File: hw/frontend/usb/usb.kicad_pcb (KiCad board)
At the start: 6 copper layers, 100 x 100 mm, 260 parts, among them J1 USB3_MICRO_AB, J2 USB3_MICRO_AB, J3 BARREL_JACK, J4 SAMTEC_QSH-090-D, P4 CONN_1, P5 CONN_1, P6 CONN_1, P7 CONN_1, P8 CONN_1, Q1 MOSFET_P, Q2 MOSFET_P, U1 TUSB1310A, U10 TPS62420, U11 TPS54821, U12 ON_CAT24C256, U13 TCA6416ARTW, U14 TCA6416ARTW, U2 TPS2065C-2, U3 GSG-IP4220CZ6, U4 USB3_ESD_SON50-10, U5 TUSB1310A, U6 TPS2065C-2, U7 GSG-IP4220CZ6, U8 USB3_ESD_SON50-10, U9 MIC5207YM5, X1 40M, X2 40M

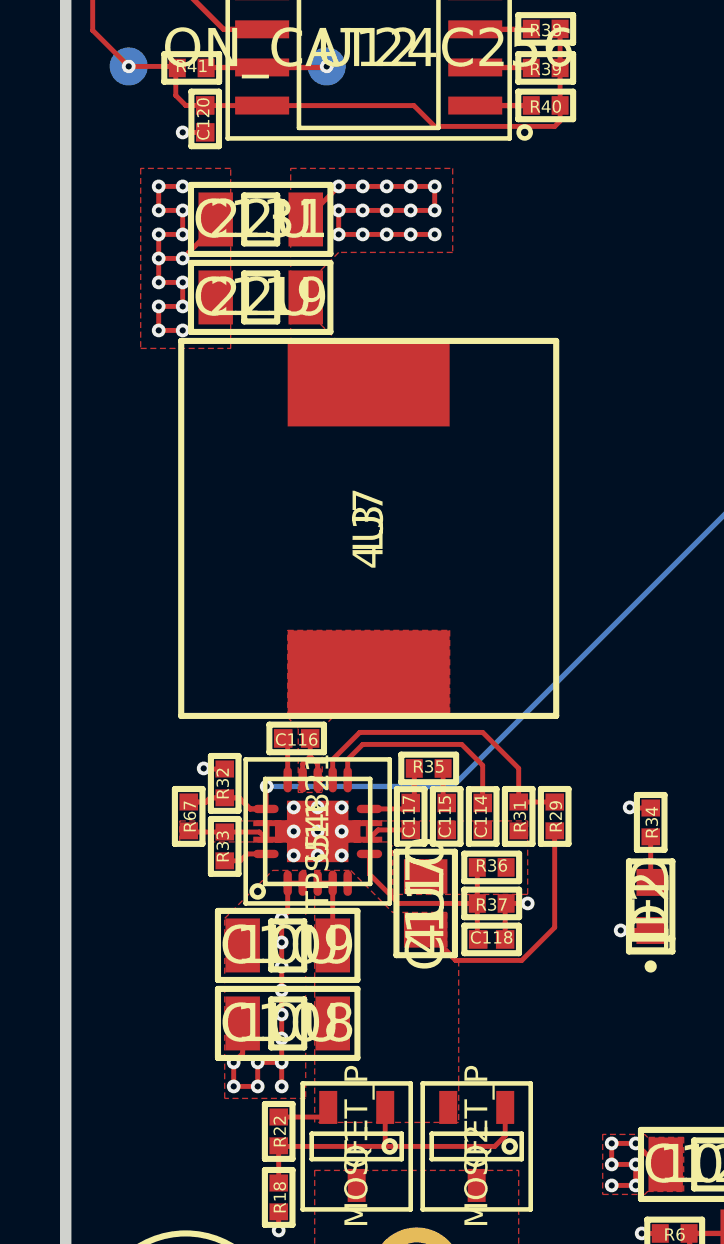
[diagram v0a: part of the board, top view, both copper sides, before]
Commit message: pull ADDR up to VRAW_SW instead of V1P8
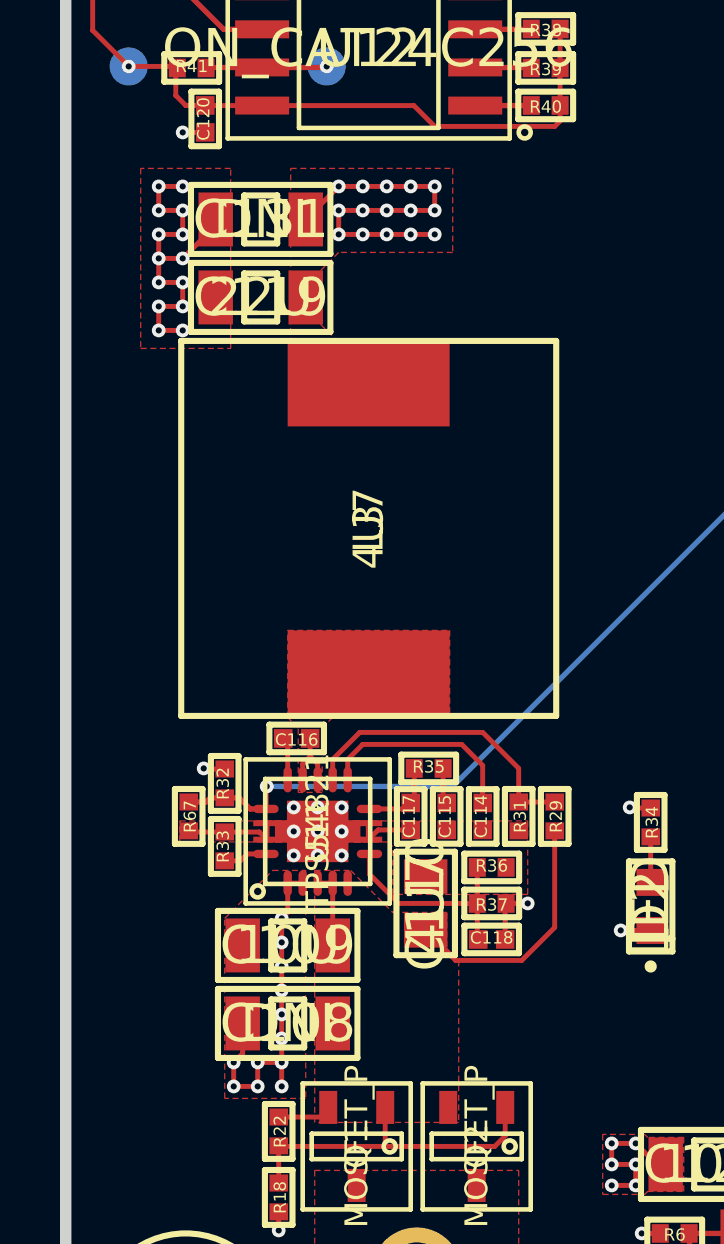
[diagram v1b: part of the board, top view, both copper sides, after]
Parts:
- C108: value 10U -> DNI
- C115: value 27N -> 82N
- C117: value 330P -> 1N5
- C118: value 470P -> 220P
- C131: value 22U -> DNI
- R18, R22: value ? -> 30K
- R21: value ? -> 180K
- R24: value ? -> 360K
- R33: value 86K6 -> 52K3
- R35: value 715R -> 1K58
- R37: value 16K5 -> 16K2
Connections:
- J3 pad 3: (no net) -> Net-(J3-Pad3)
- J4 pad 10: (no net) -> Net-(J4-Pad10)
- J4 pad 145: (no net) -> Net-(J4-Pad145)
- J4 pad 5: (no net) -> Net-(J4-Pad5)
- J4 pad 58: (no net) -> Net-(J4-Pad58)
- J4 pad 9: (no net) -> Net-(J4-Pad9)
- U1 pad A14: (no net) -> Net-(U1-PadA14)
- U1 pad C13: (no net) -> Net-(U1-PadC13)
- U1 pad C14: (no net) -> Net-(U1-PadC14)
- U1 pad D10: (no net) -> Net-(U1-PadD10)
- U1 pad D11: (no net) -> Net-(U1-PadD11)
- U1 pad D5: (no net) -> Net-(U1-PadD5)
- U1 pad D6: (no net) -> Net-(U1-PadD6)
- U1 pad E11: (no net) -> Net-(U1-PadE11)
- U1 pad E12: (no net) -> Net-(U1-PadE12)
- U1 pad F11: (no net) -> Net-(U1-PadF11)
- U1 pad G11: (no net) -> Net-(U1-PadG11)
- U1 pad H12: (no net) -> Net-(U1-PadH12)
- U1 pad J12: (no net) -> Net-(U1-PadJ12)
- U1 pad J4: (no net) -> Net-(U1-PadJ4)
- U1 pad K4: (no net) -> Net-(U1-PadK4)
- U1 pad L6: (no net) -> Net-(U1-PadL6)
- U13 pad 1: (no net) -> Net-(U13-Pad1)
- U13 pad 2: (no net) -> Net-(U13-Pad2)
- U13 pad 4: (no net) -> Net-(U13-Pad4)
- U13 pad 5: (no net) -> Net-(U13-Pad5)
- U14 pad 18: V1P8 -> VRAW_SW
- U3 pad 6: (no net) -> Net-(U3-Pad6)
- U5 pad A14: (no net) -> Net-(U5-PadA14)
- U5 pad C13: (no net) -> Net-(U5-PadC13)
- U5 pad C14: (no net) -> Net-(U5-PadC14)
- U5 pad D10: (no net) -> Net-(U5-PadD10)
- U5 pad D11: (no net) -> Net-(U5-PadD11)
- U5 pad D5: (no net) -> Net-(U5-PadD5)
- U5 pad D6: (no net) -> Net-(U5-PadD6)
- U5 pad E11: (no net) -> Net-(U5-PadE11)
- U5 pad E12: (no net) -> Net-(U5-PadE12)
- U5 pad F11: (no net) -> Net-(U5-PadF11)
- U5 pad G11: (no net) -> Net-(U5-PadG11)
- U5 pad H12: (no net) -> Net-(U5-PadH12)
- U5 pad J12: (no net) -> Net-(U5-PadJ12)
- U5 pad J4: (no net) -> Net-(U5-PadJ4)
- U5 pad K4: (no net) -> Net-(U5-PadK4)
- U5 pad L6: (no net) -> Net-(U5-PadL6)
- U7 pad 6: (no net) -> Net-(U7-Pad6)
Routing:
- net VRAW_SW: track 50.5 -> 51.5 mm, vias 36 -> 37
- net V1P8: track 102.6 -> 101.7 mm, vias 90 -> 89

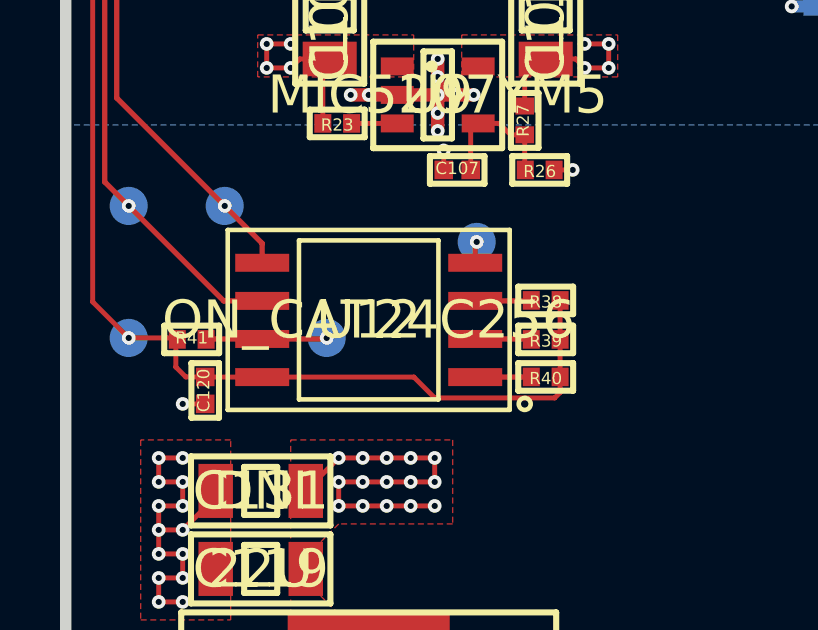
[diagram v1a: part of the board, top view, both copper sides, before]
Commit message: changed U12 (EEPROM) footprint to match selected part
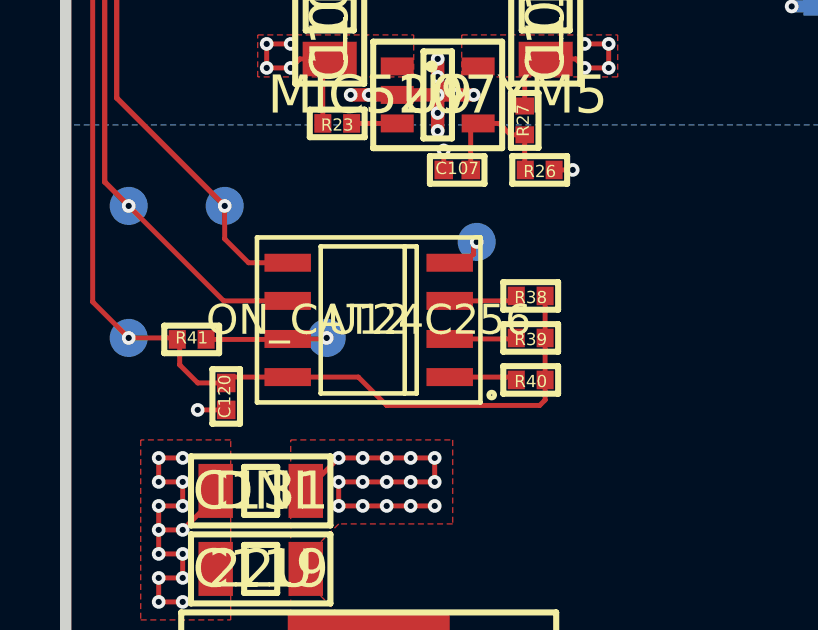
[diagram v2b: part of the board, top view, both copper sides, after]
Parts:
- U12: footprint ipc_soic:IPC_SOIC127P780X205-8N -> ipc_soic:IPC_SOIC127P600X175-8N
- moved C120 0.73 mm to (82.8, 96.5)
- moved R38 0.52 mm to (93.0, 93.2)
- moved R40 0.51 mm to (93.0, 96.0)
- moved R39 0.50 mm to (93.0, 94.6)
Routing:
- net /main_board_if/FE_I2C_SDA: track 45.2 -> 47.1 mm
- net GND: track 291.5 -> 293.3 mm
- net /main_board_if/EEPROM_VCC: track 69.8 -> 71.5 mm
- net /main_board_if/FE_I2C_SCL: track 50.6 -> 51.7 mm
- net /main_board_if/EEPROM_A2: track 1.88 -> 2.76 mm
- net /main_board_if/EEPROM_A1: track 1.88 -> 2.57 mm
- net /main_board_if/EEPROM_A0: track 1.87 -> 2.57 mm
- net /main_board_if/EEPROM_WP: track 4.04 -> 4.72 mm

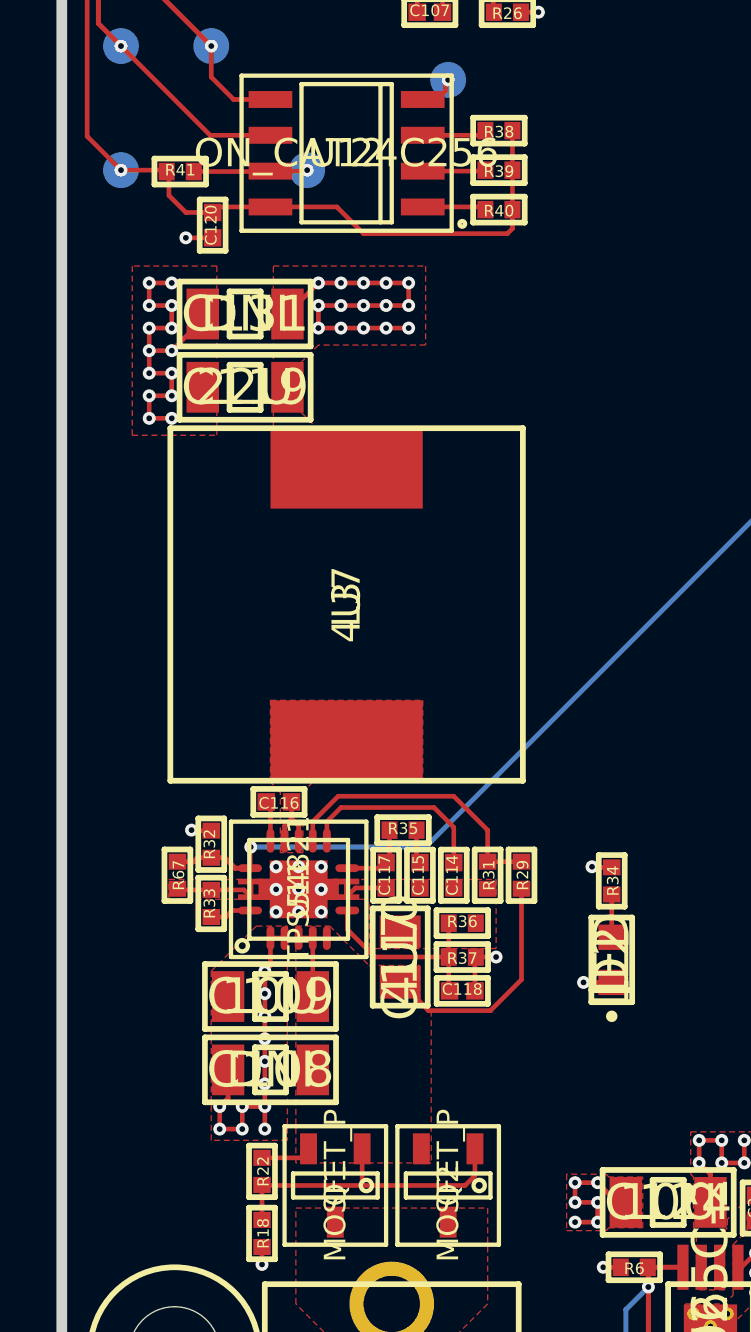
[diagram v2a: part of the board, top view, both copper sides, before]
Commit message: changed C116 to 0603, pulled zones back from U11 pins for solderability
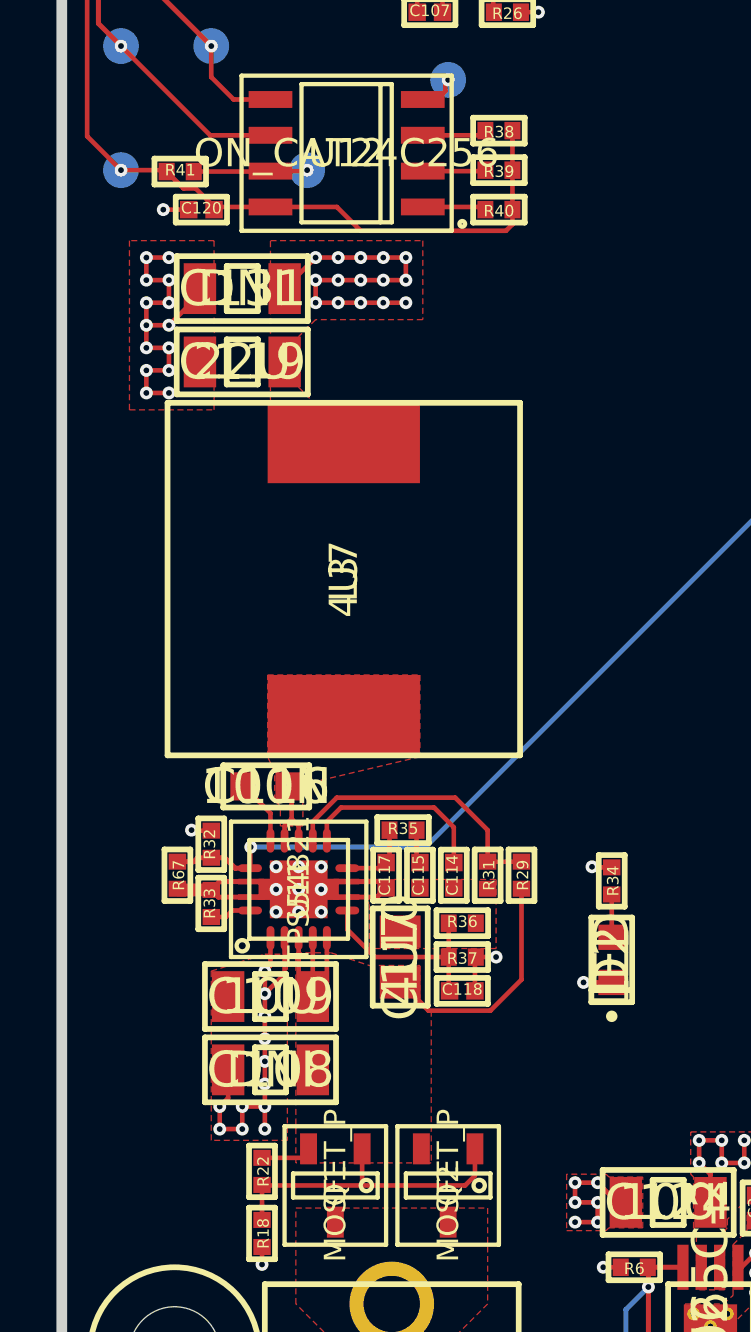
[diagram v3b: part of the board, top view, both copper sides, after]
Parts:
- C116: footprint ipc_capc1005x55n:IPC_CAPC1005X55N -> ipc_capc1608x90n:IPC_CAPC1608X90N
- moved C131 0.91 mm to (83.9, 98.8)
- moved L3 0.91 mm to (87.5, 109.1)
- moved C119 0.91 mm to (83.9, 101.4)
- moved C116 0.71 mm to (84.8, 116.5)
- moved C120 0.68 mm to (82.5, 96.0), turned to 180 degrees
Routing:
- net GND: track 293.3 -> 308.4 mm
- net /power/SW_PVIN: track 12.8 -> 17.3 mm
- net Net-(C116-Pad1): track 1.44 -> 2.88 mm
- net /power/SW_PH: track 2.36 -> 3.05 mm
